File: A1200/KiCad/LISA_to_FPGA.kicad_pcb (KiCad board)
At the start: 4 copper layers, 64 x 37 mm, 36 parts, among them J1 Conn_01x01, J2 Conn_01x40, U1 LM1117-3.3, U2 74LVC162244ADGG, U3 74LVC162244ADGG, U4 LISA, U5 RP2354B

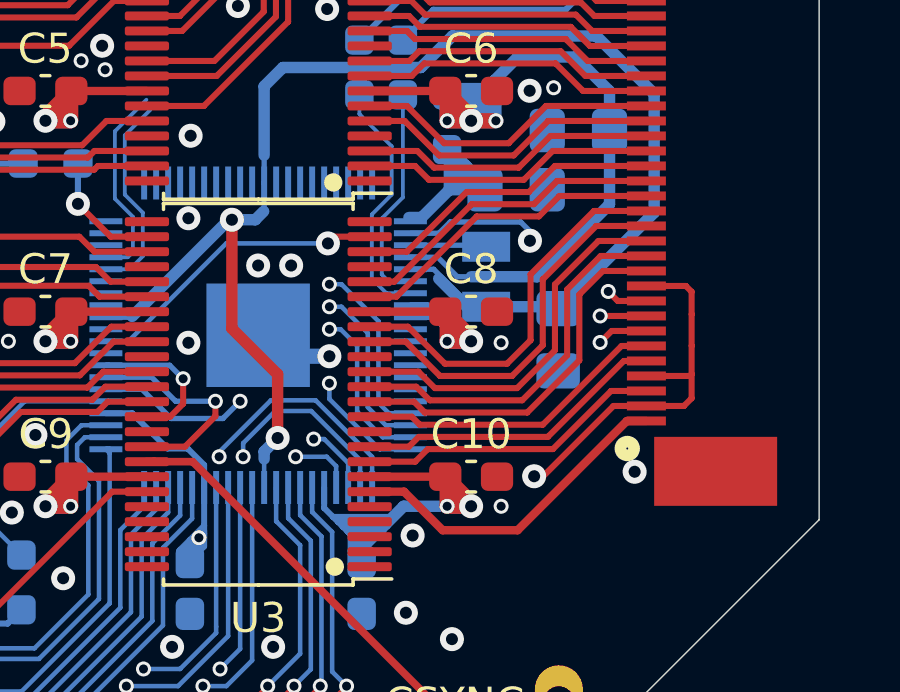
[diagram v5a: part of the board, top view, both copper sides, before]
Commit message: Add decoupling cap for pin 76 on QFN-80 footprint
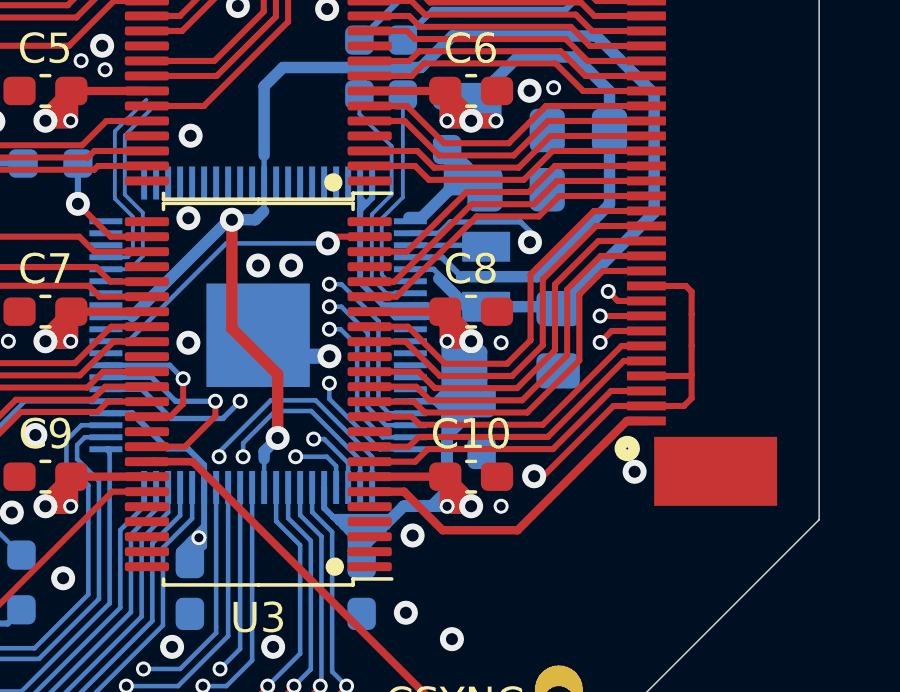
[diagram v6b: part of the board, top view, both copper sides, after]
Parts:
- added C16: 0.1uF, Capacitor_SMD:C_0603_1608Metric_Pad1.08x0.95mm_HandSolder, B.Cu at (201.0, 97.9)
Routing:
- net 3V3: track 152.7 -> 198.4 mm

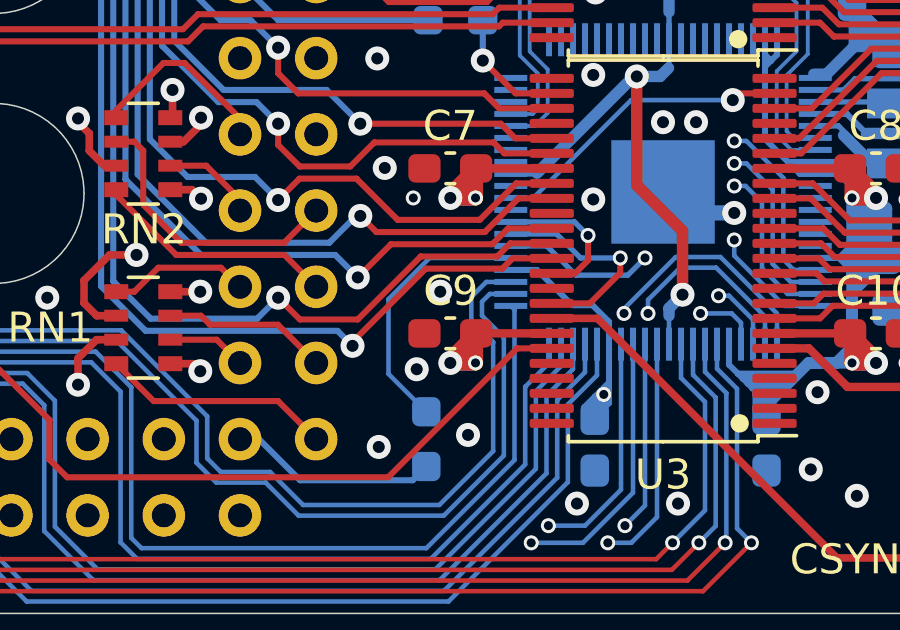
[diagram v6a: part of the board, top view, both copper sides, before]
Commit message: Add decoupling cap for pin 24 on QFN-80 footprint
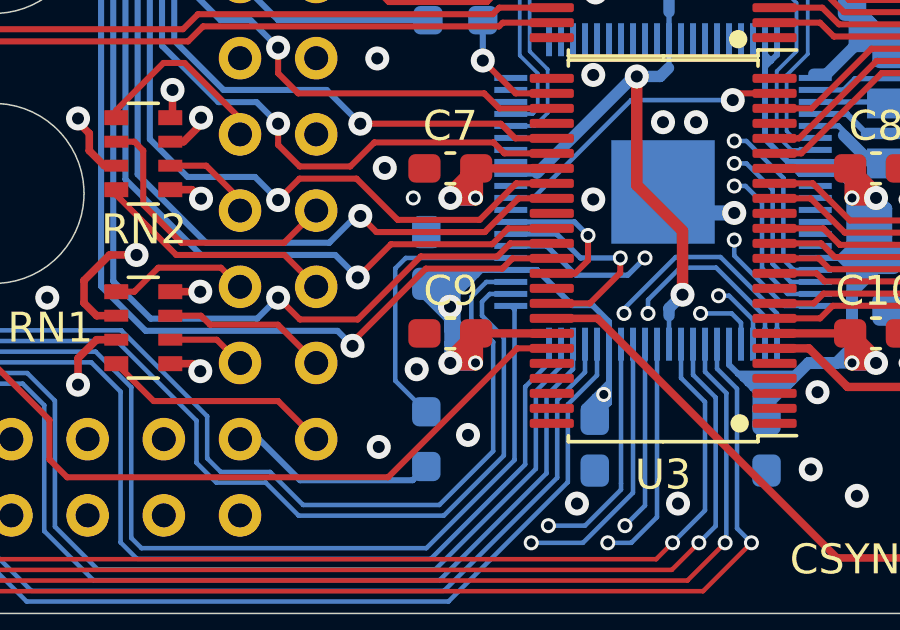
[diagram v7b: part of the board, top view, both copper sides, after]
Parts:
- added C17: 0.1uF, Capacitor_SMD:C_0603_1608Metric_Pad1.08x0.95mm_HandSolder, B.Cu at (185.7, 97.1)
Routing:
- net 3V3: track 198.4 -> 222.6 mm

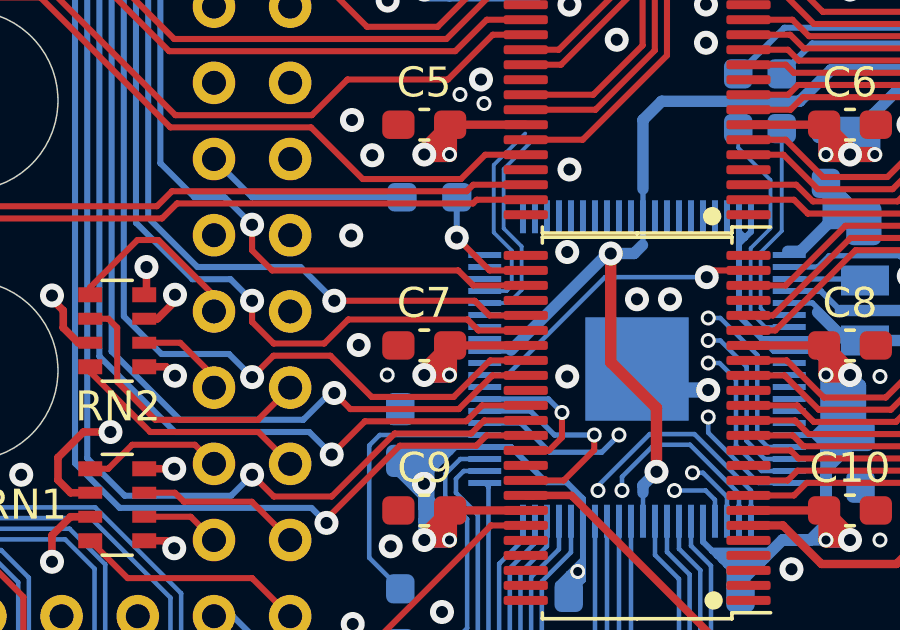
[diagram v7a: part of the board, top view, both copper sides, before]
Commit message: Add decoupling cap for pin 32 on QFN-80 footprint
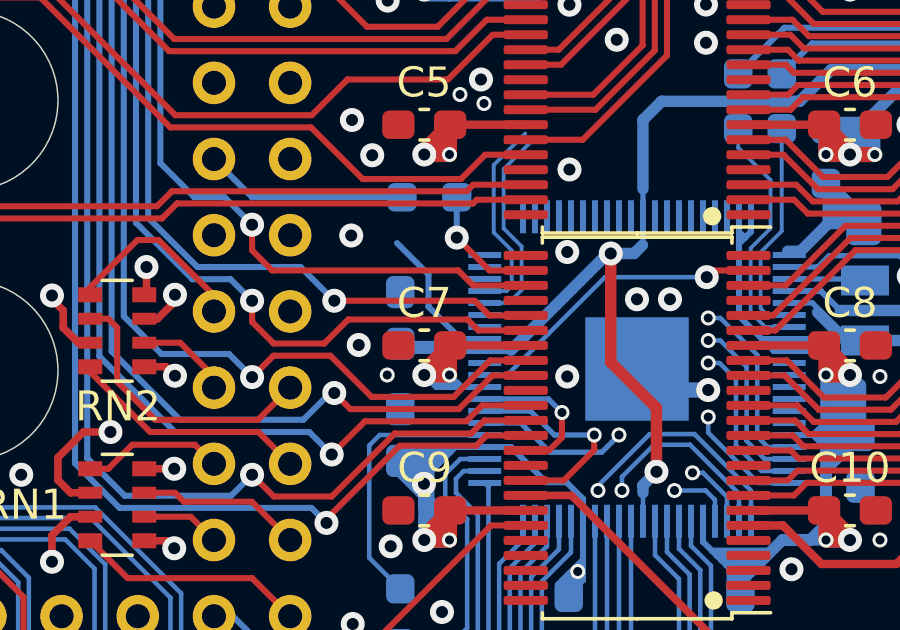
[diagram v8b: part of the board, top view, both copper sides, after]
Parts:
- added C18: 0.1uF, Capacitor_SMD:C_0603_1608Metric_Pad1.08x0.95mm_HandSolder, B.Cu at (185.7, 93.2)
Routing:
- net 1V1: track 50.8 -> 57.6 mm
- net /SWCLK: track 0.00 -> 4.88 mm
- net 3V3: track 222.6 -> 226.6 mm
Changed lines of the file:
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@@
     (thickness 1.6)
     (drawings 18)
-    (tracks 1393)
+    (tracks 1414)
     (zones 0)
-    (modules 38)
+    (modules 39)
     (nets 188)
   )
@@
   )
   (module Capacitor_SMD:C_0603_1608Metric_Pad1.08x0.95mm_HandSolder (layer B.Cu)
-    (at 185.672 97.083 270)
+    (at 185.672 93.183 270)
     (descr "Capacitor SMD 0603 (1608 Metric), square (rectangular) end terminal, IPC_7351 nominal with elongated pad for handsoldering. (Body size source: IPC-SM-782 page 76, https://www.pcb-3d.com/wordpress/wp-content/uploads/ipc-sm-782a_amendment_1_and_2.pdf), generated with kicad-footprint-generator")
     (tags "capacitor handsolder")
     (attr smd)
-    (fp_text reference C17 (at 0 -1.34 270 unlocked) (layer B.SilkS)
+    (fp_text reference C18 (at 0 -1.34 270 unlocked) (layer B.SilkS)
       (effects (font (size 1 1) (thickness 0.15)) (justify mirror))
     )
@@
       (effects (font (size 1 1) (thickness 0.15)) (justify mirror))
     )
+    (fp_line (start 1.65 -0.73) (end -1.65 -0.73) (layer B.CrtYd) (width 0.05))
+    (fp_line (start 1.65 0.73) (end 1.65 -0.73) (layer B.CrtYd) (width 0.05))
+    (fp_line (start -1.65 0.73) (end 1.65 0.73) (layer B.CrtYd) (width 0.05))
+    (fp_line (start -1.65 -0.73) (end -1.65 0.73) (layer B.CrtYd) (width 0.05))
+    (fp_line (start -0.146267 -0.51) (end 0.146267 -0.51) (layer B.SilkS) (width 0.12))
+    (fp_line (start -0.146267 0.51) (end 0.146267 0.51) (layer B.SilkS) (width 0.12))
+    (fp_line (start 0.8 -0.4) (end -0.8 -0.4) (layer B.Fab) (width 0.1))
+    (fp_line (start 0.8 0.4) (end 0.8 -0.4) (layer B.Fab) (width 0.1))
+    (fp_line (start -0.8 0.4) (end 0.8 0.4) (layer B.Fab) (width 0.1))
+    (fp_line (start -0.8 -0.4) (end -0.8 0.4) (layer B.Fab) (width 0.1))
     (fp_text user %R (at 0 0 90) (layer B.Fab) hide
       (effects (font (size 0.4 0.4) (thickness 0.06)) (justify mirror))
     )
+    (pad 2 smd roundrect (at 0.8625 0 270) (size 1.075 0.95) (layers B.Cu B.Paste B.Mask) (roundrect_rratio 0.25)
+      (net 158 1V1))
+    (pad 1 smd roundrect (at -0.8625 0 270) (size 1.075 0.95) (layers B.Cu B.Paste B.Mask) (roundrect_rratio 0.25)
+      (net 2 GND))
+    (model ${KISYS3DMOD}/Capacitor_SMD.3dshapes/C_0603_1608Metric.wrl
+      (at (xyz 0 0 0))
+      (scale (xyz 1 1 1))
+      (rotate (xyz 0 0 0))
+    )
+  )
+  (module Capacitor_SMD:C_0603_1608Metric_Pad1.08x0.95mm_HandSolder (layer B.Cu)
+    (at 185.672 97.083 270)
+    (descr "Capacitor SMD 0603 (1608 Metric), square (rectangular) end terminal, IPC_7351 nominal with elongated pad for handsoldering. (Body size source: IPC-SM-782 page 76, https://www.pcb-3d.com/wordpress/wp-content/uploads/ipc-sm-782a_amendment_1_and_2.pdf), generated with kicad-footprint-generator")
+    (tags "capacitor handsolder")
+    (attr smd)
+    (fp_text reference C17 (at 0 -1.34 270 unlocked) (layer B.SilkS)
+      (effects (font (size 1 1) (thickness 0.15)) (justify mirror))
+    )
+    (fp_text value 0.1uF (at 0 -1.43 90) (layer B.Fab) hide
+      (effects (font (size 1 1) (thickness 0.15)) (justify mirror))
+    )
     (fp_line (start -0.8 -0.4) (end -0.8 0.4) (layer B.Fab) (width 0.1))
     (fp_line (start -0.8 0.4) (end 0.8 0.4) (layer B.Fab) (width 0.1))
@@
     (fp_line (start 1.65 0.73) (end 1.65 -0.73) (layer B.CrtYd) (width 0.05))
     (fp_line (start 1.65 -0.73) (end -1.65 -0.73) (layer B.CrtYd) (width 0.05))
+    (fp_text user %R (at 0 0 90) (layer B.Fab) hide
+      (effects (font (size 0.4 0.4) (thickness 0.06)) (justify mirror))
+    )
     (pad 2 smd roundrect (at 0.8625 0 270) (size 1.075 0.95) (layers B.Cu B.Paste B.Mask) (roundrect_rratio 0.25)
       (net 3 3V3))
@@
   (segment (start 186.462 98.533) (end 187.0495 97.9455) (width 0.2) (layer B.Cu) (net 3))
   (segment (start 186.462 98.708) (end 186.462 98.533) (width 0.2) (layer B.Cu) (net 3))
+  (segment (start 188.487 95.483) (end 187.712 95.483) (width 0.2) (layer B.Cu) (net 3))
+  (segment (start 186.871999 95.482999) (end 186.472 95.083) (width 0.2) (layer B.Cu) (net 3))
+  (segment (start 187.712 95.483) (end 186.871999 95.482999) (width 0.2) (layer B.Cu) (net 3))
+  (segment (start 186.747 95.358) (end 186.472 95.083) (width 0.2) (layer B.Cu) (net 3))
+  (segment (start 187.587 95.358) (end 186.747 95.358) (width 0.2) (layer B.Cu) (net 3))
+  (segment (start 187.712 95.483) (end 187.587 95.358) (width 0.2) (layer B.Cu) (net 3))
+  (segment (start 187.587 95.358) (end 187.312 95.083) (width 0.2) (layer B.Cu) (net 3))
   (segment (start 190.0977 99.0973) (end 189.8545 99.0973) (width 0.2794) (layer F.Cu) (net 4))
   (segment (start 190.10479 99.09021) (end 190.0977 99.0973) (width 0.2794) (layer F.Cu) (net 4))
@@
   (segment (start 203.218292 98.271459) (end 205.74955 95.7402) (width 0.2032) (layer F.Cu) (net 153))
   (segment (start 205.74955 95.7402) (end 206.5048 95.7402) (width 0.2032) (layer F.Cu) (net 153))
+  (segment (start 188.487 93.883) (end 187.687 93.883) (width 0.2) (layer B.Cu) (net 156))
+  (segment (start 187.687 93.883) (end 186.612 92.808) (width 0.2) (layer B.Cu) (net 156))
+  (segment (start 186.612 92.808) (end 186.612 91.733) (width 0.2) (layer B.Cu) (net 156))
+  (segment (start 186.612 91.733) (end 185.562 90.683) (width 0.2) (layer B.Cu) (net 156))
   (segment (start 199.012 90.958) (end 198.587 90.958) (width 0.381) (layer B.Cu) (net 157))
   (segment (start 199.937 90.033) (end 199.012 90.958) (width 0.381) (layer B.Cu) (net 157))
@@
   (segment (start 201.162 93.933) (end 203.4995 93.933) (width 0.381) (layer B.Cu) (net 158))
   (segment (start 193.762 89.808) (end 193.762 90.583782) (width 0.1778) (layer B.Cu) (net 158))
-  (segment (start 189.262782 94.283) (end 188.487 94.283) (width 0.1778) (layer B.Cu) (net 158))
   (segment (start 193.762 89.808) (end 193.762 88.883) (width 0.1778) (layer B.Cu) (net 158))
   (segment (start 200.519097 93.932999) (end 199.580701 92.994603) (width 0.381) (layer B.Cu) (net 158))
@@
   (segment (start 204.837 84.908) (end 200.037 84.908) (width 0.381) (layer B.Cu) (net 158))
   (segment (start 203.562 93.9955) (end 206.762 90.7955) (width 0.381) (layer B.Cu) (net 158))
+  (segment (start 185.9095 94.283) (end 185.672 94.0455) (width 0.2) (layer B.Cu) (net 158))
+  (segment (start 189.337 94.283) (end 189.362 94.258) (width 0.2) (layer B.Cu) (net 158))
+  (segment (start 188.487 94.283) (end 189.337 94.283) (width 0.2) (layer B.Cu) (net 158))
+  (segment (start 185.672 94.0455) (end 187.2495 94.0455) (width 0.2) (layer B.Cu) (net 158))
+  (segment (start 187.487 94.283) (end 187.637 94.283) (width 0.2) (layer B.Cu) (net 158))
+  (segment (start 187.637 94.283) (end 185.9095 94.283) (width 0.2) (layer B.Cu) (net 158))
+  (segment (start 188.487 94.283) (end 187.637 94.283) (width 0.2) (layer B.Cu) (net 158))
+  (segment (start 187.362 94.158) (end 185.7845 94.158) (width 0.2) (layer B.Cu) (net 158))
+  (segment (start 185.7845 94.158) (end 185.672 94.0455) (width 0.2) (layer B.Cu) (net 158))
+  (segment (start 187.2495 94.0455) (end 187.362 94.158) (width 0.2) (layer B.Cu) (net 158))
+  (segment (start 187.362 94.158) (end 187.487 94.283) (width 0.2) (layer B.Cu) (net 158))
   (segment (start 201.112 91.883) (end 201.162 91.933) (width 0.1778) (layer B.Cu) (net 159))
   (segment (start 198.637 91.883) (end 201.112 91.883) (width 0.1778) (layer B.Cu) (net 159))
